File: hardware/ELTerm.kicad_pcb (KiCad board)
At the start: 2 copper layers, 81.6 x 44.5 mm, 31 parts, among them J1 Barrel_Jack_Switch, J2 Conn_02x10_Odd_Even, J3 Conn_01x02, J4 Mini-DIN-6, J5 Conn_02x03_Odd_Even, J6 Conn_01x02, J7 DB9_Male_MountingHoles, SW1 SW_Push, U1 SY8120, U2 Pico, U3 MAX3232, U4 NC7WZ16P6X

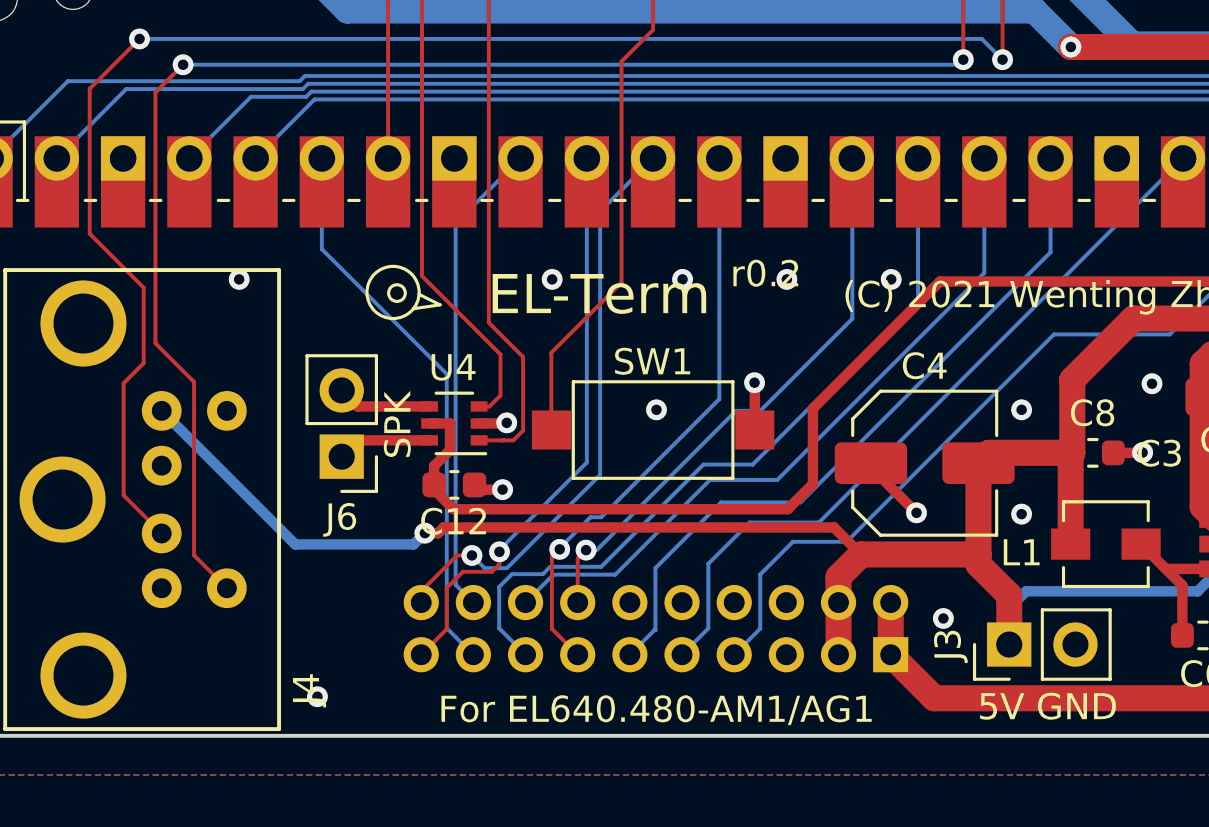
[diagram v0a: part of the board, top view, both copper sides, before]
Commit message: - Fix PCB EL pin assignment
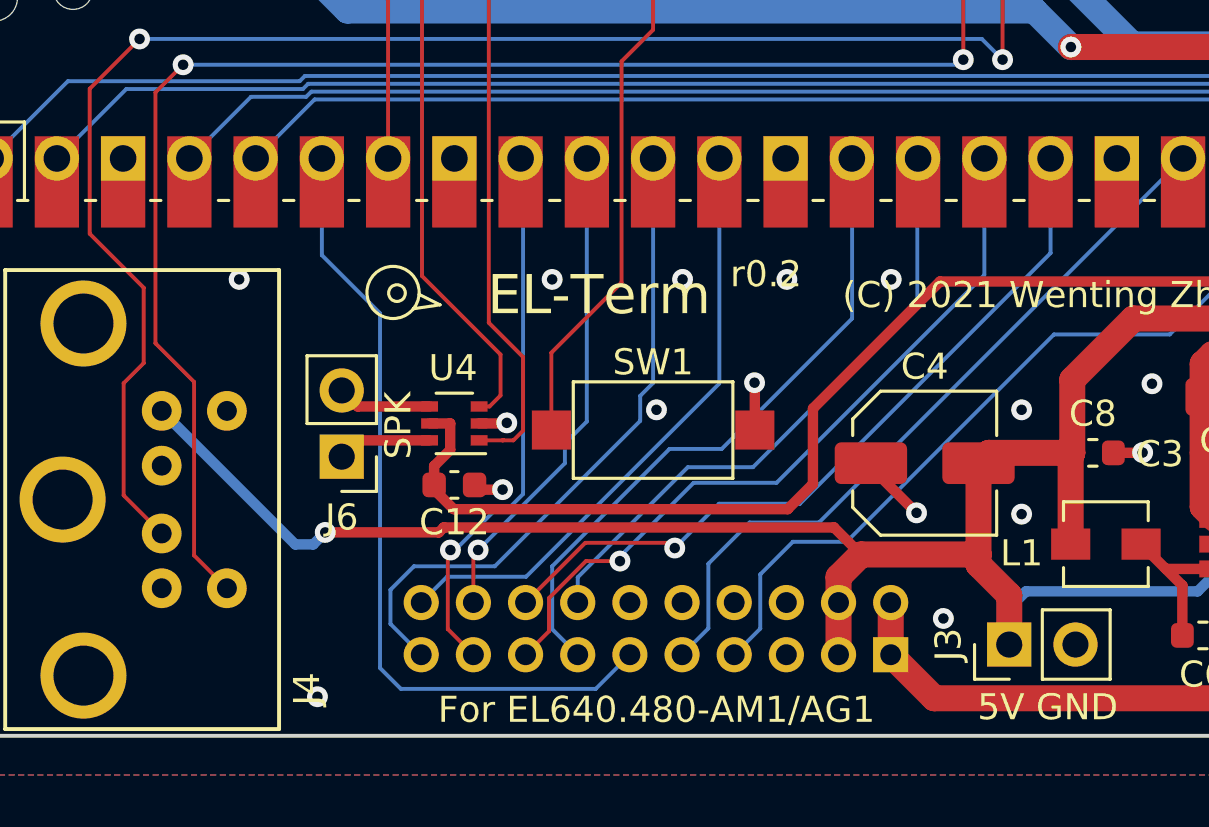
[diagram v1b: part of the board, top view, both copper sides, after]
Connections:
- U2 pad 10: /UD1 -> /UD2
- U2 pad 11: /UD0 -> /UD1
- U2 pad 12: /LD3 -> /UD0
- U2 pad 14: /LD2 -> /LD3
- U2 pad 15: /LD1 -> /LD2
- U2 pad 16: /LD0 -> /LD1
- U2 pad 17: /VCLK -> /LD0
- U2 pad 6: /UD3 -> /VCLK
- U2 pad 9: /UD2 -> /UD3
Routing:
- net /VCLK: track 27.5 -> 30.9 mm
- net /UD1: track 22.3 -> 25.5 mm, vias 1 -> 0
- net /LD3: track 22.3 -> 25.4 mm, vias 1 -> 0
- net /LD0: track 27.2 -> 29.5 mm, vias 0 -> 1
- net /LD2: track 22.2 -> 23.9 mm, vias 1 -> 0
- net /UD0: track 22.5 -> 23.5 mm, vias 1 -> 0
- net /UD2: track 18.3 -> 18.8 mm, vias 0 -> 1
- net /UD3: track 21.4 -> 21.0 mm, vias 0 -> 1
- net /LD1: track 29.0 -> 28.9 mm, vias 0 -> 1
